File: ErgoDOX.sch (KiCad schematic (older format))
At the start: 111 parts, among them J1 USB, J2 3.5mm, J3 JMP, J4 JMP, J5 JMP, J6 JMP, SW1 SWITCH_PUSH, SW10 SWITCH_PUSH, SW11 SWITCH_PUSH, SW12 SWITCH_PUSH, SW13 SWITCH_PUSH, SW14 SWITCH_PUSH, SW15 SWITCH_PUSH, SW16 SWITCH_PUSH, SW17 SWITCH_PUSH, SW18 SWITCH_PUSH, SW19 SWITCH_PUSH, SW2 SWITCH_PUSH, SW20 SWITCH_PUSH, SW21 SWITCH_PUSH, SW22 SWITCH_PUSH, SW23 SWITCH_PUSH, SW24 SWITCH_PUSH, SW25 SWITCH_PUSH, SW26 SWITCH_PUSH, SW27 SWITCH_PUSH, SW28 SWITCH_PUSH, SW29 SWITCH_PUSH, SW3 SWITCH_PUSH, SW30 SWITCH_PUSH, SW31 SWITCH_PUSH, SW32 SWITCH_PUSH, SW33 SWITCH_PUSH, SW34 SWITCH_PUSH, SW35 SWITCH_PUSH, SW36 SWITCH_PUSH, SW37 SWITCH_PUSH, SW38 SWITCH_PUSH, SW39 SWITCH_PUSH, SW4 SWITCH_PUSH, SW40 SWITCH_PUSH, SW41 SWITCH_PUSH, SW42 SWITCH_PUSH, SW43 SWITCH_PUSH, SW44 SWITCH_PUSH, SW45 SWITCH_PUSH, SW46 SWITCH_PUSH, SW5 SWITCH_PUSH, SW6 SWITCH_PUSH, SW7 SWITCH_PUSH, SW8 SWITCH_PUSH, SW9 SWITCH_PUSH, U1 ProMicro

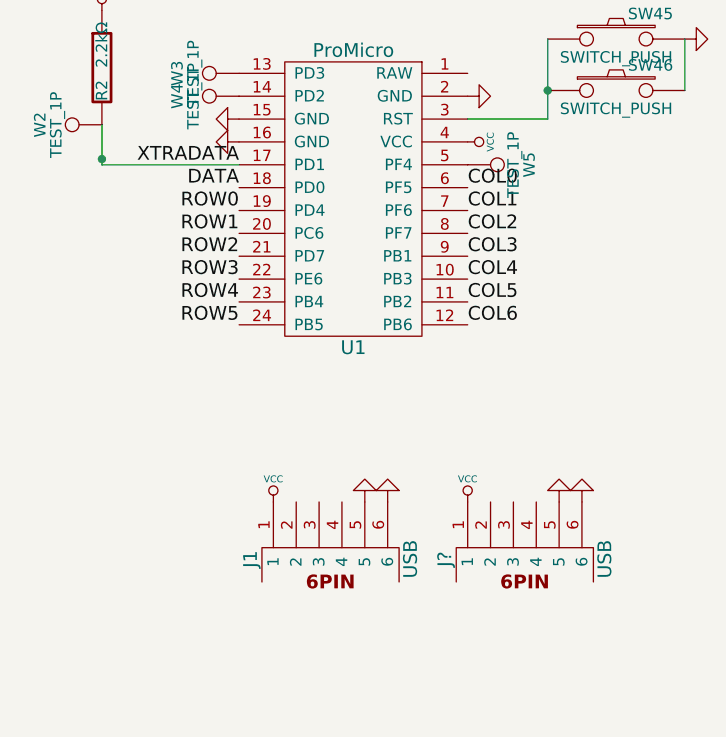
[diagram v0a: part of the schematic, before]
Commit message: initial traces complete
dont judge me on the thumb section i'm not crazy about how weird the wire traces are either.
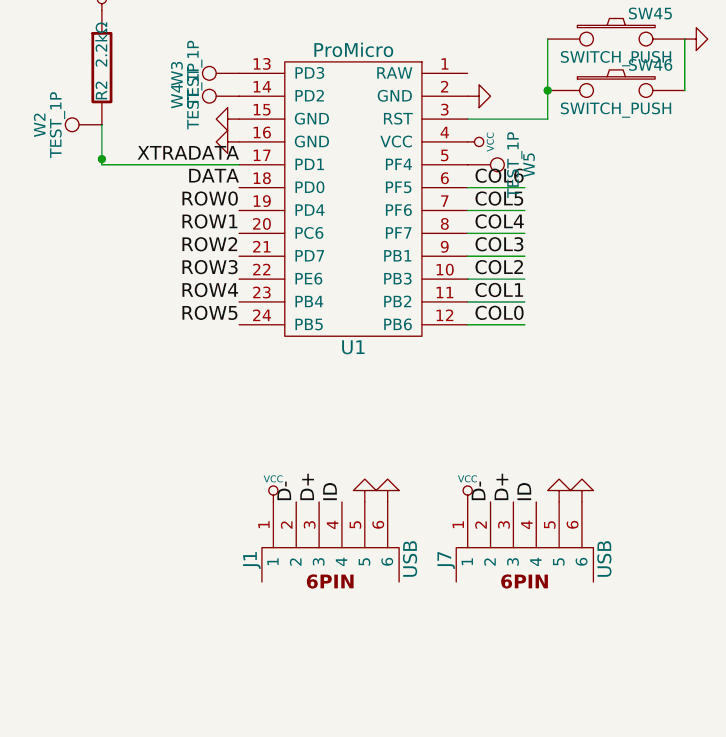
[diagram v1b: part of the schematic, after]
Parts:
- gave numbers to parts that had none: 1
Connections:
- net COL0: now also U1.12 (PB6); no longer U1.6 (PF5)
- net COL1: now also U1.11 (PB2); no longer U1.7 (PF6)
- net COL2: now also U1.10 (PB3); no longer U1.8 (PF7)
- net COL4: now also U1.8 (PF7); no longer U1.10 (PB3)
- net COL5: now also U1.7 (PF6); no longer U1.11 (PB2)
- net COL6: now also U1.6 (PF5); no longer U1.12 (PB6)
- net D-: now reaches J1.2
- net D-: now also J7.2
- net D+: now reaches J1.3
- net D+: now also J7.3
- net ID: now reaches J1.4
- net ID: now also J7.4
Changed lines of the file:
@@
 Text Label 3100 9850 3    60   ~ 0
 COL4
-Text Label 7875 3000 0    60   ~ 0
+Text Label 8125 3400 2    60   ~ 0
 COL1
 Text Label 1825 3600 1    60   ~ 0
@@
 LED_C
 $Comp
-L GND #PWR01
+L GND #PWR2
 U 1 1 4FD4C15E
 P 1825 4550
-F 0 "#PWR01" H 1825 4550 30  0001 C CNN
+F 0 "#PWR2" H 1825 4550 30  0001 C CNN
 F 1 "GND" H 1825 4480 30  0001 C CNN
 F 2 "" H 1825 4550 60  0001 C CNN
@@
 $EndComp
 $Comp
-L GND #PWR02
+L GND #PWR4
 U 1 1 4FD4C191
 P 2075 4550
-F 0 "#PWR02" H 2075 4550 30  0001 C CNN
+F 0 "#PWR4" H 2075 4550 30  0001 C CNN
 F 1 "GND" H 2075 4480 30  0001 C CNN
 F 2 "" H 2075 4550 60  0001 C CNN
@@
 $EndComp
 $Comp
-L GND #PWR03
+L GND #PWR6
 U 1 1 4FD4C1B3
 P 2325 4550
-F 0 "#PWR03" H 2325 4550 30  0001 C CNN
+F 0 "#PWR6" H 2325 4550 30  0001 C CNN
 F 1 "GND" H 2325 4480 30  0001 C CNN
 F 2 "" H 2325 4550 60  0001 C CNN
@@
 $EndComp
 $Comp
-L VCC #PWR04
+L VCC #PWR17
 U 1 1 4FD9DC69
 P 7875 2700
-F 0 "#PWR04" H 7875 2800 30  0001 C CNN
+F 0 "#PWR17" H 7875 2800 30  0001 C CNN
 F 1 "VCC" H 7875 2800 30  0000 C CNN
 F 2 "" H 7875 2700 60  0001 C CNN
@@
 $EndComp
 $Comp
-L VCC #PWR05
+L VCC #PWR11
 U 1 1 4FD9DD5F
 P 6275 2125
-F 0 "#PWR05" H 6275 2225 30  0001 C CNN
+F 0 "#PWR11" H 6275 2225 30  0001 C CNN
 F 1 "VCC" H 6275 2225 30  0000 C CNN
 F 2 "" H 6275 2125 60  0001 C CNN
@@
 $EndComp
 $Comp
-L VCC #PWR06
+L VCC #PWR1
 U 1 1 4FD9DD6B
 P 1500 3525
-F 0 "#PWR06" H 1500 3625 30  0001 C CNN
+F 0 "#PWR1" H 1500 3625 30  0001 C CNN
 F 1 "VCC" H 1500 3625 30  0000 C CNN
 F 2 "" H 1500 3525 60  0001 C CNN
@@
 Text Label 6875 3000 2    60   ~ 0
 ROW0
-Text Label 7875 3500 0    60   ~ 0
+Text Label 8125 2900 2    60   ~ 0
 COL6
-Text Label 7875 3400 0    60   ~ 0
+Text Label 8125 3000 2    60   ~ 0
 COL5
-Text Label 7875 2900 0    60   ~ 0
+Text Label 8125 3500 2    60   ~ 0
 COL0
-Text Label 7875 3100 0    60   ~ 0
+Text Label 8125 3300 2    60   ~ 0
 COL2
-Text Label 7875 3200 0    60   ~ 0
+Text Label 8125 3200 2    60   ~ 0
 COL3
-Text Label 7875 3300 0    60   ~ 0
+Text Label 8125 3100 2    60   ~ 0
 COL4
 $Comp
@@
 $EndComp
 $Comp
-L GND #PWR07
+L GND #PWR3
 U 1 1 4FD9EC6B
 P 2050 1575
-F 0 "#PWR07" H 2050 1575 30  0001 C CNN
+F 0 "#PWR3" H 2050 1575 30  0001 C CNN
 F 1 "GND" H 2050 1505 30  0001 C CNN
 F 2 "" H 2050 1575 60  0001 C CNN
@@
 $EndComp
 $Comp
-L GND #PWR08
+L GND #PWR8
 U 1 1 4FD9EC71
 P 4200 1600
-F 0 "#PWR08" H 4200 1600 30  0001 C CNN
+F 0 "#PWR8" H 4200 1600 30  0001 C CNN
 F 1 "GND" H 4200 1530 30  0001 C CNN
 F 2 "" H 4200 1600 60  0001 C CNN
@@
 $EndComp
 $Comp
-L VCC #PWR09
+L VCC #PWR5
 U 1 1 4FD9EC77
 P 2300 1575
-F 0 "#PWR09" H 2300 1675 30  0001 C CNN
+F 0 "#PWR5" H 2300 1675 30  0001 C CNN
 F 1 "VCC" H 2300 1675 30  0000 C CNN
 F 2 "" H 2300 1575 60  0001 C CNN
@@
 $EndComp
 $Comp
-L VCC #PWR010
+L VCC #PWR7
 U 1 1 4FD9EC7D
 P 3950 1600
-F 0 "#PWR010" H 3950 1700 30  0001 C CNN
+F 0 "#PWR7" H 3950 1700 30  0001 C CNN
 F 1 "VCC" H 3950 1700 30  0000 C CNN
 F 2 "" H 3950 1600 60  0001 C CNN
@@
 $EndComp
 $Comp
-L GND #PWR011
+L GND #PWR16
 U 1 1 4FFF4219
 P 7525 4225
-F 0 "#PWR011" H 7525 4225 30  0001 C CNN
+F 0 "#PWR16" H 7525 4225 30  0001 C CNN
 F 1 "GND" H 7525 4155 30  0001 C CNN
 F 2 "" H 7525 4225 60  0001 C CNN
@@
 $EndComp
 $Comp
-L VCC #PWR012
-U 1 1 4FFF4300
-P 7025 4275
-F 0 "#PWR012" H 7025 4375 30  0001 C CNN
-F 1 "VCC" H 7025 4375 30  0000 C CNN
-F 2 "" H 7025 4275 60  0001 C CNN
-F 3 "" H 7025 4275 60  0001 C CNN
-	1    7025 4275
-	1    0    0    -1
-$EndComp
-$Comp
-L GND #PWR013
+L GND #PWR15
 U 1 1 4FFF43E7
 P 7425 4225
-F 0 "#PWR013" H 7425 4225 30  0001 C CNN
+F 0 "#PWR15" H 7425 4225 30  0001 C CNN
 F 1 "GND" H 7425 4155 30  0001 C CNN
 F 2 "" H 7425 4225 60  0001 C CNN
@@
 $EndComp
 $Comp
-L VCC #PWR014
+L VCC #PWR10
 U 1 1 500D128D
 P 5650 1350
-F 0 "#PWR014" H 5650 1450 30  0001 C CNN
+F 0 "#PWR10" H 5650 1450 30  0001 C CNN
 F 1 "VCC" H 5650 1450 30  0000 C CNN
 F 2 "" H 5650 1350 60  0001 C CNN
@@
 $EndComp
 $Comp
-L GND #PWR015
+L GND #PWR9
 U 1 1 500D12B7
 P 5600 1700
-F 0 "#PWR015" H 5600 1700 30  0001 C CNN
+F 0 "#PWR9" H 5600 1700 30  0001 C CNN
 F 1 "GND" H 5600 1630 30  0001 C CNN
 F 2 "" H 5600 1700 60  0001 C CNN
@@
 $EndComp
 $Comp
-L GND #PWR016
+L GND #PWR13
 U 1 1 5B04150C
 P 6825 2700
-F 0 "#PWR016" H 6825 2700 30  0001 C CNN
+F 0 "#PWR13" H 6825 2700 30  0001 C CNN
 F 1 "GND" H 6825 2630 30  0001 C CNN
 F 2 "" H 6825 2700 60  0001 C CNN
@@
 $EndComp
 $Comp
-L GND #PWR017
+L GND #PWR12
 U 1 1 5B0416D7
 P 6825 2600
-F 0 "#PWR017" H 6825 2600 30  0001 C CNN
+F 0 "#PWR12" H 6825 2600 30  0001 C CNN
 F 1 "GND" H 6825 2530 30  0001 C CNN
 F 2 "" H 6825 2600 60  0001 C CNN
@@
 $EndComp
 $Comp
-L GND #PWR018
+L GND #PWR19
 U 1 1 5B0417A2
 P 7925 2500
-F 0 "#PWR018" H 7925 2500 30  0001 C CNN
+F 0 "#PWR19" H 7925 2500 30  0001 C CNN
 F 1 "GND" H 7925 2430 30  0001 C CNN
 F 2 "" H 7925 2500 60  0001 C CNN
@@
 	8825 2475 8825 2250
 $Comp
-L GND #PWR019
+L GND #PWR22
 U 1 1 5B0576DC
 P 8875 2250
-F 0 "#PWR019" H 8875 2250 30  0001 C CNN
+F 0 "#PWR22" H 8875 2250 30  0001 C CNN
 F 1 "GND" H 8875 2180 30  0001 C CNN
 F 2 "" H 8875 2250 60  0001 C CNN
@@
 XTRADATA
 $Comp
-L 6PIN J?
+L 6PIN J7
 U 1 1 5B069BBC
 P 8125 4475
-F 0 "J?" H 8075 4825 60  0000 C CNN
+F 0 "J7" H 8075 4825 60  0000 C CNN
 F 1 "USB" H 8075 4125 60  0000 C CNN
 F 2 "BishopKicadConsolidated:USB_miniB_hirose_5S8" H 8125 4475 60  0001 C CNN
@@
 $EndComp
 $Comp
-L GND #PWR?
+L GND #PWR21
 U 1 1 5B069BC2
 P 8375 4225
-F 0 "#PWR?" H 8375 4225 30  0001 C CNN
+F 0 "#PWR21" H 8375 4225 30  0001 C CNN
 F 1 "GND" H 8375 4155 30  0001 C CNN
 F 2 "" H 8375 4225 60  0001 C CNN
@@
 $EndComp
 $Comp
-L VCC #PWR?
+L GND #PWR20
+U 1 1 5B069BCE
+P 8275 4225
+F 0 "#PWR20" H 8275 4225 30  0001 C CNN
+F 1 "GND" H 8275 4155 30  0001 C CNN
+F 2 "" H 8275 4225 60  0001 C CNN
+F 3 "" H 8275 4225 60  0001 C CNN
+	1    8275 4225
+	-1   0    0    1
+$EndComp
+$Comp
+L VCC #PWR18
 U 1 1 5B069BC8
 P 7875 4275
-F 0 "#PWR?" H 7875 4375 30  0001 C CNN
+F 0 "#PWR18" H 7875 4375 30  0001 C CNN
 F 1 "VCC" H 7875 4375 30  0000 C CNN
 F 2 "" H 7875 4275 60  0001 C CNN
@@
 $EndComp
 $Comp
-L GND #PWR?
-U 1 1 5B069BCE
-P 8275 4225
-F 0 "#PWR?" H 8275 4225 30  0001 C CNN
-F 1 "GND" H 8275 4155 30  0001 C CNN
-F 2 "" H 8275 4225 60  0001 C CNN
-F 3 "" H 8275 4225 60  0001 C CNN
-	1    8275 4225
-	-1   0    0    1
-$EndComp
+L VCC #PWR14
+U 1 1 4FFF4300
+P 7025 4275
+F 0 "#PWR14" H 7025 4375 30  0001 C CNN
+F 1 "VCC" H 7025 4375 30  0000 C CNN
+F 2 "" H 7025 4275 60  0001 C CNN
+F 3 "" H 7025 4275 60  0001 C CNN
+	1    7025 4275
+	1    0    0    -1
+$EndComp
+Text Label 7125 4275 1    60   ~ 0
+D-
+Text Label 7225 4275 1    60   ~ 0
+D+
+Text Label 7325 4275 1    60   ~ 0
+ID
+Text Label 7975 4275 1    60   ~ 0
+D-
+Text Label 8075 4275 1    60   ~ 0
+D+
+Text Label 8175 4275 1    60   ~ 0
+ID
+Wire Wire Line
+	8125 2900 7875 2900
+Wire Wire Line
+	8125 3000 7875 3000
+Wire Wire Line
+	8125 3100 7875 3100
+Wire Wire Line
+	8125 3200 7875 3200
+Wire Wire Line
+	8125 3300 7875 3300
+Wire Wire Line
+	8125 3400 7875 3400
+Wire Wire Line
+	8125 3500 7875 3500
 $EndSCHEMATC
